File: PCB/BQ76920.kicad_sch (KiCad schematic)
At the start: 81 parts, among them CN6 WAFER-SH1.0-6PWB, Q1 CSD13381F4, Q10 TP0610K-T1-GE3, Q2 CSD13381F4, Q3 CSD13381F4, Q4 CSD13381F4, Q5 CSD13381F4, Q6 BSC0702LS, Q7 BSC0702LS, Q8 BSC0702LS, Q9 BSC0702LS, SW3 B3U-1000P, U3 TPS61240DRVR, U4 BQ7692003PW

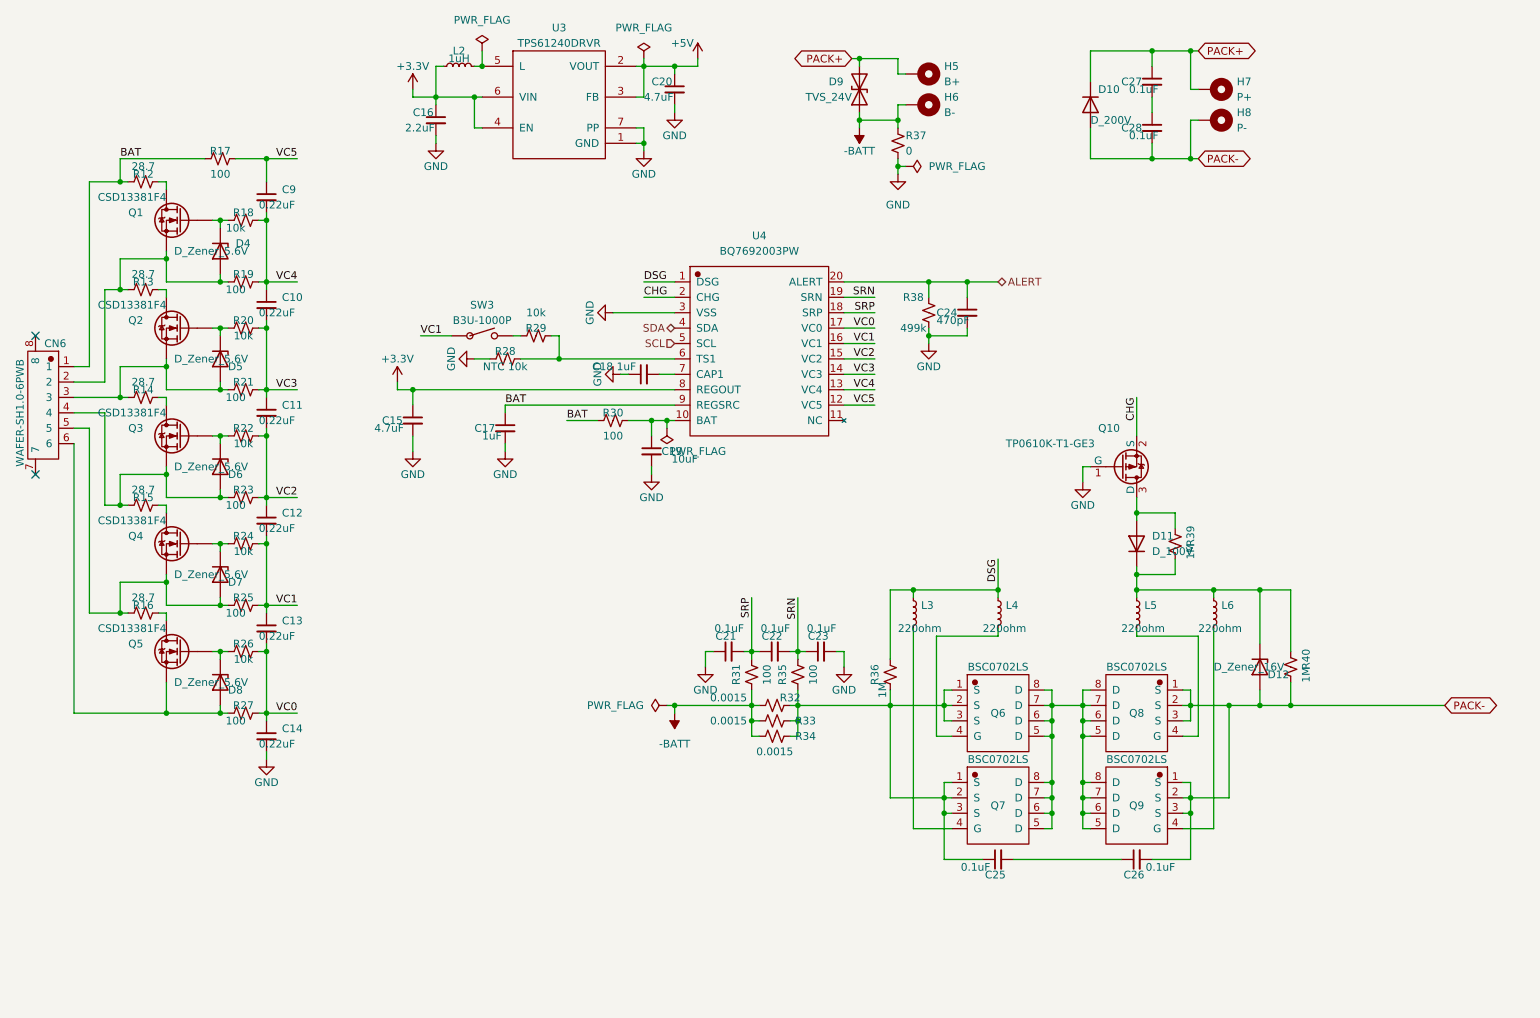
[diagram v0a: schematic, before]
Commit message: feat(PCB): 新增预充功能; 支持2路电池温度采样; 支持低功耗模式; 更换主控芯片; 采用降压输出5V
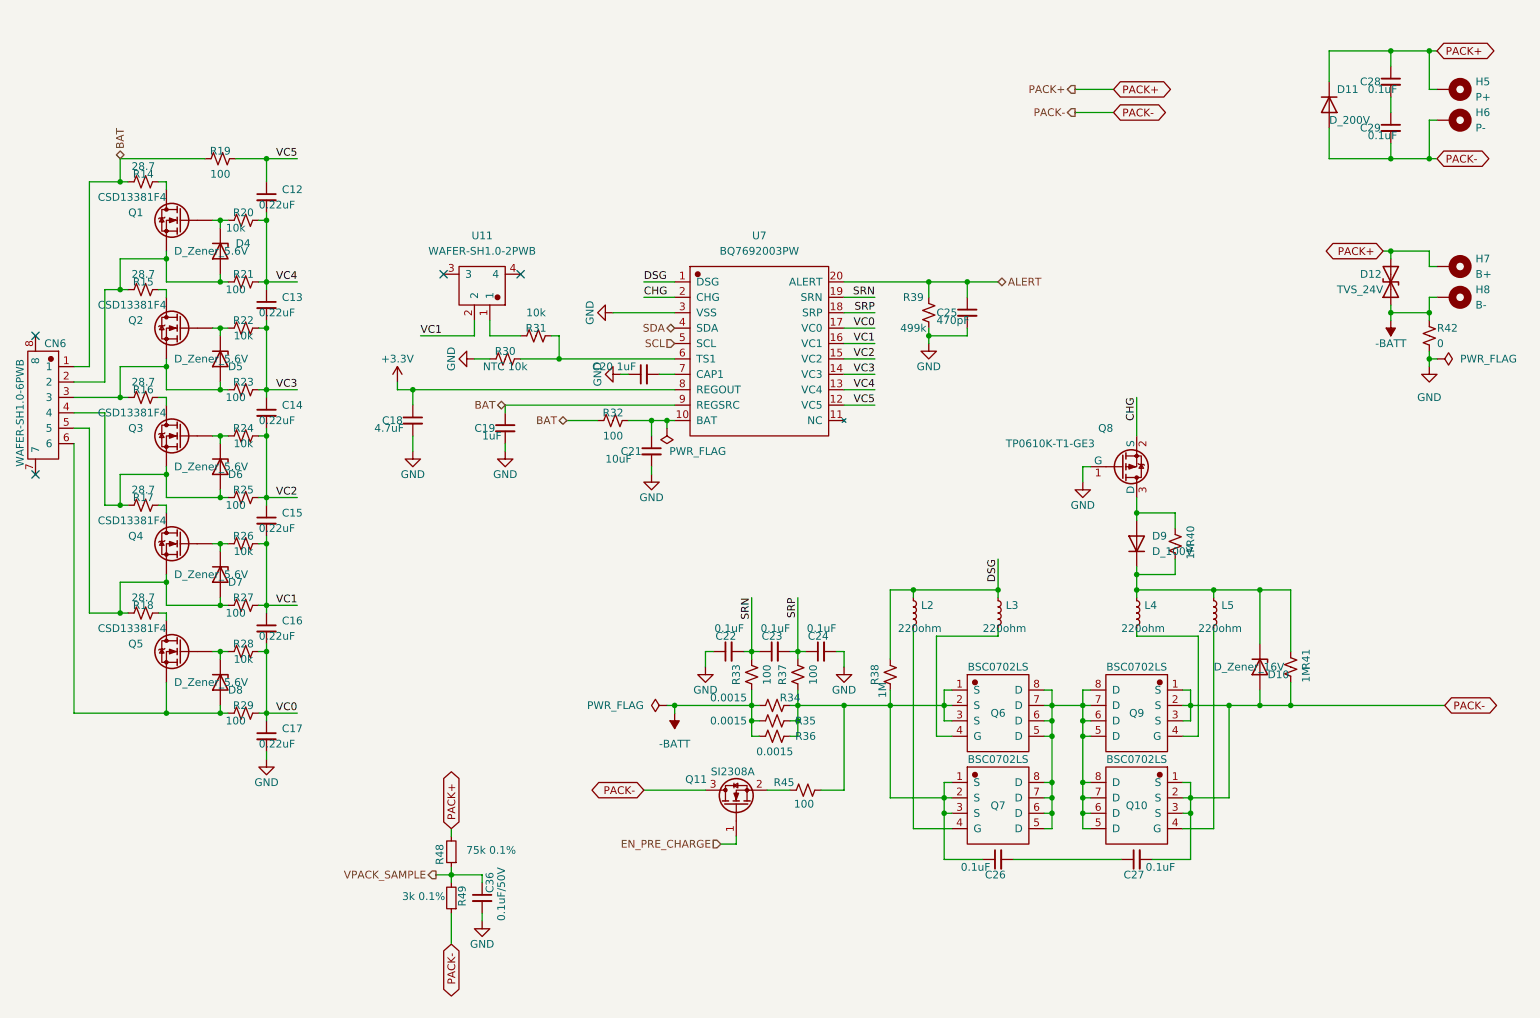
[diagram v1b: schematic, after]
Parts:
- removed C16: 2.2uF, Capacitor_SMD:C_0402_1005Metric_Pad0.74x0.62mm_HandSolder, symbol Device:C_Small
- removed C20: 4.7uF, Capacitor_SMD:C_0402_1005Metric_Pad0.74x0.62mm_HandSolder, symbol Device:C_Small
- removed L2: 1uH, Inductor_SMD:L_1210_3225Metric_Pad1.42x2.65mm_HandSolder, symbol Device:L_Small
- removed SW3: B3U-1000P, Rick_Switch:B3U-1000P, symbol Rick_Switch:B3U-1000P
- removed U3: TPS61240DRVR, Rick_DC-DC:TPS61240DRVR_WSON-6_L2.0-W2.0-P0.65-TL-EP, symbol Rick_DC-DC:TPS61240DRVR
- added C36: 0.1uF/50V, Capacitor_SMD:C_0402_1005Metric_Pad0.74x0.62mm_HandSolder, symbol Library:C_Small
- added Q11: SI2308A, Package_TO_SOT_SMD:SOT-23, symbol Library:Q_NMOS_GSD
- added R45: 100, Resistor_SMD:R_0805_2012Metric_Pad1.20x1.40mm_HandSolder, symbol Library:R_Small_US
- added R48: 75k 0.1%, Resistor_SMD:R_0402_1005Metric_Pad0.72x0.64mm_HandSolder, symbol Library:R_Small
- added R49: 3k 0.1%, Resistor_SMD:R_0402_1005Metric_Pad0.72x0.64mm_HandSolder, symbol Library:R_Small
- added U11: WAFER-SH1.0-2PWB, Rick_Connector:CONN-SMD_2P-P1.00_XUNPU_WAFER-SH1.0-2PWB, symbol Library:WAFER-SH1.0-2PWB
- C12: renamed from C9; symbol Device:C_Small -> Library:C_Small
- C13: renamed from C10; symbol Device:C_Small -> Library:C_Small
- C14: renamed from C11; symbol Device:C_Small -> Library:C_Small
- C15: renamed from C12; symbol Device:C_Small -> Library:C_Small
- C16: renamed from C13; symbol Device:C_Small -> Library:C_Small
- C17: renamed from C14; symbol Device:C_Small -> Library:C_Small
- C18: renamed from C15; symbol Device:C_Small -> Library:C_Small
- C19: renamed from C17; symbol Device:C_Small -> Library:C_Small
- C20: renamed from C18; symbol Device:C_Small -> Library:C_Small
- C21: renamed from C19; symbol Device:C_Small -> Library:C_Small
- C22: renamed from C21; symbol Device:C_Small -> Library:C_Small
- C23: renamed from C22; symbol Device:C_Small -> Library:C_Small
- C24: renamed from C23; symbol Device:C_Small -> Library:C_Small
- C25: renamed from C24; symbol Device:C_Small -> Library:C_Small
- C26: renamed from C25; symbol Device:C_Small -> Library:C_Small
- C27: renamed from C26; symbol Device:C_Small -> Library:C_Small
- C28: renamed from C27; symbol Device:C_Small -> Library:C_Small
- C29: renamed from C28; symbol Device:C_Small -> Library:C_Small
- CN6: symbol Rick_Connector:WAFER-SH1.0-6PWB -> Library:WAFER-SH1.0-6PWB
- D10: renamed from D12; symbol Device:D_Zener -> Library:D_Zener
- D11: renamed from D10; symbol Device:D -> Library:D
- D12: renamed from D9; symbol Device:D_TVS -> Library:D_TVS
- D4, D5, D6, D7, D8: symbol Device:D_Zener -> Library:D_Zener
- D9: renamed from D11; symbol Device:D -> Library:D
- H5: renamed from H7; symbol Mechanical:MountingHole_Pad -> Library:MountingHole_Pad
- H6: renamed from H8; symbol Mechanical:MountingHole_Pad -> Library:MountingHole_Pad
- H7: renamed from H5; symbol Mechanical:MountingHole_Pad -> Library:MountingHole_Pad
- H8: renamed from H6; symbol Mechanical:MountingHole_Pad -> Library:MountingHole_Pad
- L2: renamed from L3; symbol Device:L_Small -> Library:L_Small
- L3: renamed from L4; symbol Device:L_Small -> Library:L_Small
- L4: renamed from L5; symbol Device:L_Small -> Library:L_Small
- L5: renamed from L6; symbol Device:L_Small -> Library:L_Small
- Q1, Q2, Q3, Q4, Q5: symbol Rick_MOSFET:CSD13381F4 -> Library:CSD13381F4
- Q10: renamed from Q9; symbol Rick_MOSFET:BSC0702LS -> Library:BSC0702LS
- Q6, Q7: symbol Rick_MOSFET:BSC0702LS -> Library:BSC0702LS
- Q8: renamed from Q10; symbol Rick_MOSFET:TP0610K-T1-GE3 -> Library:TP0610K-T1-GE3
- Q9: renamed from Q8; symbol Rick_MOSFET:BSC0702LS -> Library:BSC0702LS
- R14: renamed from R12; symbol Device:R_Small_US -> Library:R_Small_US
- R15: renamed from R13; symbol Device:R_Small_US -> Library:R_Small_US
- R16: renamed from R14; symbol Device:R_Small_US -> Library:R_Small_US
- R17: renamed from R15; symbol Device:R_Small_US -> Library:R_Small_US
- R18: renamed from R16; symbol Device:R_Small_US -> Library:R_Small_US
- R19: renamed from R17; symbol Device:R_Small_US -> Library:R_Small_US
- R20: renamed from R18; symbol Device:R_Small_US -> Library:R_Small_US
- R21: renamed from R19; symbol Device:R_Small_US -> Library:R_Small_US
- R22: renamed from R20; symbol Device:R_Small_US -> Library:R_Small_US
- R23: renamed from R21; symbol Device:R_Small_US -> Library:R_Small_US
- R24: renamed from R22; symbol Device:R_Small_US -> Library:R_Small_US
- R25: renamed from R23; symbol Device:R_Small_US -> Library:R_Small_US
- R26: renamed from R24; symbol Device:R_Small_US -> Library:R_Small_US
- R27: renamed from R25; symbol Device:R_Small_US -> Library:R_Small_US
- R28: renamed from R26; symbol Device:R_Small_US -> Library:R_Small_US
- R29: renamed from R27; symbol Device:R_Small_US -> Library:R_Small_US
- R30: renamed from R28; symbol Device:R_Small_US -> Library:R_Small_US
- R31: renamed from R29; symbol Device:R_Small_US -> Library:R_Small_US
- R32: renamed from R30; symbol Device:R_Small_US -> Library:R_Small_US
- R33: renamed from R31; symbol Device:R_Small_US -> Library:R_Small_US
- R34: renamed from R32; symbol Device:R_Small_US -> Library:R_Small_US
- R35: renamed from R33; symbol Device:R_Small_US -> Library:R_Small_US
- R36: renamed from R34; symbol Device:R_Small_US -> Library:R_Small_US
- R37: renamed from R35; symbol Device:R_Small_US -> Library:R_Small_US
- R38: renamed from R36; symbol Device:R_Small_US -> Library:R_Small_US
- R39: renamed from R38; symbol Device:R_Small_US -> Library:R_Small_US
- R40: renamed from R39; symbol Device:R_Small_US -> Library:R_Small_US
- R41: renamed from R40; symbol Device:R_Small_US -> Library:R_Small_US
- R42: renamed from R37; symbol Device:R_Small_US -> Library:R_Small_US
- U7: renamed from U4; symbol Rick_BMS:BQ7692003PW -> Library:BQ7692003PW
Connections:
- net GND: now also C36.2
- net PACK+: now also R48.2
- net PACK-: now also Q11.3 (D), R49.1
- net SRN: now also C22.2, C23.1, R33.2; no longer C23.2, C24.1, R37.2
- net SRP: now also C23.2, C24.1, R37.2; no longer C22.2, C23.1, R33.2
- net VC1: now also U11.2
- net at C26.1, Q6.1 (S), Q6.2 (S)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: now also R45.2
- net at R31.1: now also U11.1
- new net: Q11.2 (S), R45.1
- new net EN_PRE_CHARGE: Q11.1 (G)
- new net VPACK_SAMPLE: C36.1, R48.1, R49.2
- no-connect marks 2 -> 4
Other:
- moved on the sheet: C28, C29, D11, D12, H5, H6, H7, H8, R42

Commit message: fix(PCB): 调优放电/预充电阻功率与母线采样布局
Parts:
- added R12: 10k, Resistor_SMD:R_0402_1005Metric_Pad0.72x0.64mm_HandSolder, symbol Library:R_Small_US
- C19, C20: value 1uF -> 1uF 50V
- C21: value 10uF -> 10uF 50V
- C22, C23, C24, C26, C27, C28, C29: value 0.1uF -> 0.1uF 50V
- C36: value 0.1uF/50V -> 0.1uF 50V
- D10: value D_Zener_16V -> BZX585-B16,115
- D11: value D_200V -> ES1D
- D12: value TVS_24V -> SMAJ24CA
- D4, D5, D6, D7, D8: value D_Zener_5.6V -> EDZVT2R5.6B
- D9: value D_100V -> 1N4148WS T4
- H5, H6, H7, H8: now not fitted
- L2, L3, L4, L5: value 220ohm -> BLM18EG221SN1D
- Q11: value SI2308A -> AO3400A
- R14, R15, R16, R17, R18: footprint Resistor_SMD:R_0402_1005Metric_Pad0.72x0.64mm_HandSolder -> Resistor_SMD:R_2010_5025Metric_Pad1.40x2.65mm_HandSolder
- R30: value NTC 10k -> NCP15XH103F03RC
- R33, R37: value 100 -> 100 0.1%
- R34, R35, R36: value 0.0015 -> HoJLRX2512-2W-1.5mR-1%
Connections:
- net EN_PRE_CHARGE: now also R12.1
- net GND: now also R49.1, R12.2
- net PACK+: no longer R48.2
- net PACK-: now also R48.2; no longer R49.1
- net SRN: now also C23.2, C24.1, R37.2; no longer C22.2, C23.1, R33.2
- net SRP: now also C22.2, C23.1, R33.2; no longer C23.2, C24.1, R37.2
